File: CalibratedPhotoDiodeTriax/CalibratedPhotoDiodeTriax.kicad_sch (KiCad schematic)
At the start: 0 parts

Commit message: Deleted old pcb
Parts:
- added J1: TO-5 Photodiode Socket: Conn_01x03, Package_TO_SOT_THT:TO-5-3, symbol Connector_Generic:Conn_01x03
- added J2: CBJ70 Triax Throughhole Connector, KiCADv6:CONN_CBJ70_CIN, symbol Connector:Conn_Triaxial
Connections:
- new net: J1.1 (Pin_1), J2.1 (In1)
- new net: J1.2 (Pin_2), J2.2 (In2)
- new net GND: J1.3 (Pin_3), J2.3 (Ext)

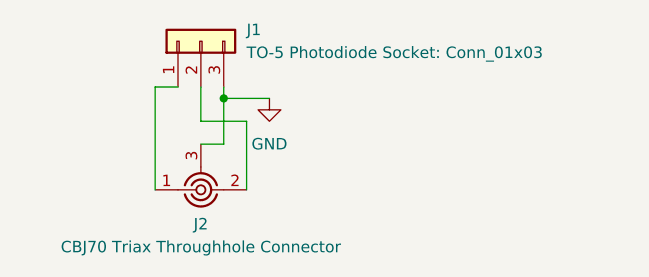
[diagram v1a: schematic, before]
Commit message: Swapped traces on triax connector
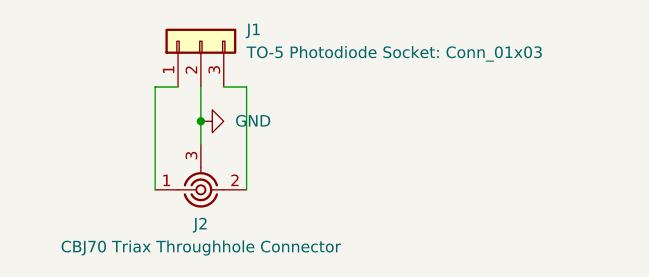
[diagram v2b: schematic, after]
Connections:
- net GND: now also J1.2 (Pin_2); no longer J1.3 (Pin_3)
- net at J2.2 (In2): now also J1.3 (Pin_3); no longer J1.2 (Pin_2)
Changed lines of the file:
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@@
 	(paper "A4")
 	(junction
-		(at 157.48 60.96)
+		(at 154.94 63.5)
 		(diameter 0)
 		(color 0 0 0 0)
@@
 	(wire
 		(pts
-			(xy 154.94 63.5) (xy 154.94 59.69)
-		)
-		(stroke
-			(width 0)
-			(type default)
-		)
-	)
-	(wire
-		(pts
-			(xy 157.48 66.04) (xy 157.48 60.96)
-		)
-		(stroke
-			(width 0)
-			(type default)
-		)
-	)
-	(wire
-		(pts
-			(xy 160.02 71.12) (xy 160.02 63.5)
+			(xy 160.02 59.69) (xy 160.02 71.12)
 		)
 		(stroke
@@
 	(wire
 		(pts
-			(xy 160.02 63.5) (xy 154.94 63.5)
-		)
-		(stroke
-			(width 0)
-			(type default)
-		)
-	)
-	(wire
-		(pts
-			(xy 157.48 60.96) (xy 157.48 59.69)
-		)
-		(stroke
-			(width 0)
-			(type default)
-		)
-	)
-	(wire
-		(pts
-			(xy 154.94 66.04) (xy 157.48 66.04)
-		)
-		(stroke
-			(width 0)
-			(type default)
-		)
-	)
-	(wire
-		(pts
-			(xy 157.48 60.96) (xy 162.56 60.96)
+			(xy 154.94 59.69) (xy 154.94 63.5)
 		)
 		(stroke
@@
 		(pts
 			(xy 149.86 71.12) (xy 149.86 59.69)
+		)
+		(stroke
+			(width 0)
+			(type default)
+		)
+	)
+	(wire
+		(pts
+			(xy 154.94 63.5) (xy 154.94 66.04)
+		)
+		(stroke
+			(width 0)
+			(type default)
+		)
+	)
+	(wire
+		(pts
+			(xy 160.02 59.69) (xy 157.48 59.69)
 		)
 		(stroke
@@
 	(symbol
 		(lib_id "power:GND")
-		(at 162.56 60.96 0)
+		(at 154.94 63.5 90)
 		(unit 1)
 		(exclude_from_sim no)
@@
 		(fields_autoplaced yes)
 		(property "Reference" "#PWR01"
-			(at 162.56 67.31 0)
+			(at 161.29 63.5 0)
 			(effects
 				(font
@@
 		)
 		(property "Value" "GND"
-			(at 162.56 66.04 0)
-			(effects
-				(font
-					(size 1.27 1.27)
-				)
+			(at 158.75 63.4999 90)
+			(effects
+				(font
+					(size 1.27 1.27)
+				)
+				(justify right)
 			)
 		)
 		(property "Footprint" ""
-			(at 162.56 60.96 0)
+			(at 154.94 63.5 0)
 			(effects
 				(font
@@
 		)
 		(property "Datasheet" ""
-			(at 162.56 60.96 0)
+			(at 154.94 63.5 0)
 			(effects
 				(font
@@
 		)
 		(property "Description" "Power symbol creates a global label with name \"GND\" , ground"
-			(at 162.56 60.96 0)
-			(effects
-				(font
+			(at 154.94 63.5 0)
+			(effects
+				(font
